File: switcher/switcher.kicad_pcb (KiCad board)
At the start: 2 copper layers, 50 x 100 mm, 61 parts, among them J1 DCDC, J10 GP3, J11 I1, J12 I2, J13 I3, J14 Barrel_Jack_Switch, J2 USB_B_Micro, J3 Power, J4 UART, J5 O1, J6 O2, J7 O3, J8 GP1, J9 GP2, Q1 BC549, Q2 BC549, Q3 BC549, Q4 BC549, Q5 BC549, Q8 BC549, U1 ESP-12E

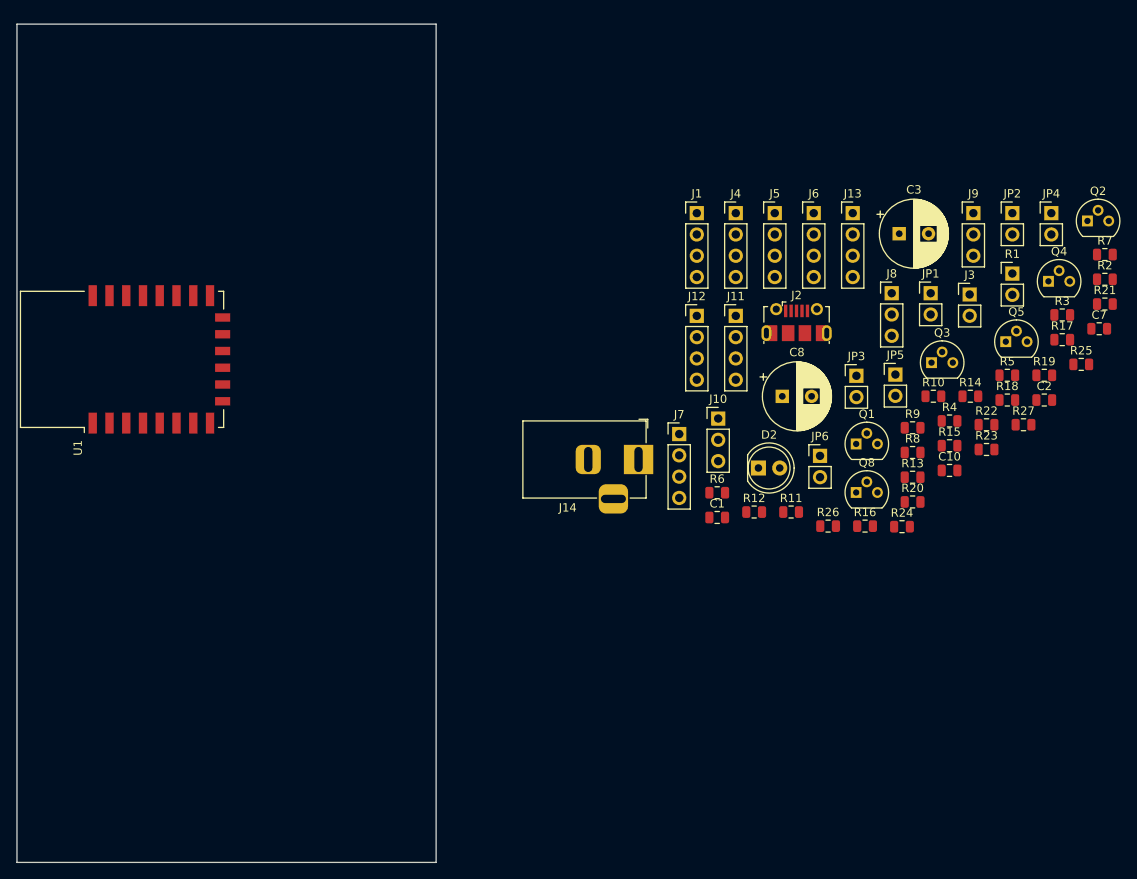
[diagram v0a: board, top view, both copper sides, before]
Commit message: finish the switcher pcb
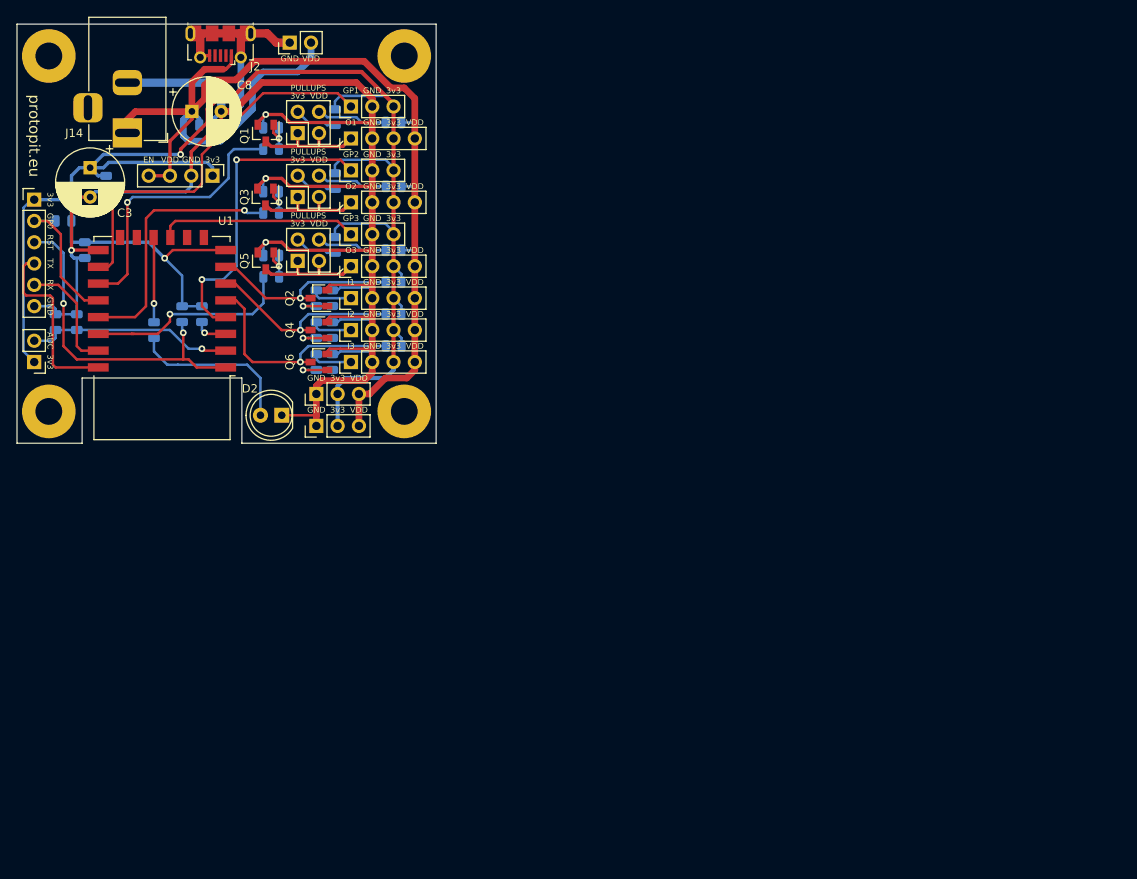
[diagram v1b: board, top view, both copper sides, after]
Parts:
- removed JP4, JP6: USE_VDD, Connector_PinHeader_2.54mm:PinHeader_1x02_P2.54mm_Vertical
- removed JP5: USE_3v3, Connector_PinHeader_2.54mm:PinHeader_1x02_P2.54mm_Vertical
- removed Q8: BC549, Package_TO_SOT_THT:TO-92
- added J16: POWER_OUT, Connector_PinHeader_2.54mm:PinHeader_1x03_P2.54mm_Vertical, F.Cu at (79.7, 100.3)
- added J17: DEBUG, Connector_PinHeader_2.54mm:PinHeader_1x06_P2.54mm_Vertical, F.Cu at (46.0, 73.3)
- added Q6: BC817, Package_TO_SOT_SMD:SOT-23, F.Cu at (80.0, 92.7)
- added REF**: MountingHole_3.2mm_M3_Pad, MountingHole:MountingHole_3.2mm_M3_Pad, F.Cu at (90.2, 98.6)
- added REF**: MountingHole_3.2mm_M3_Pad, MountingHole:MountingHole_3.2mm_M3_Pad, F.Cu at (47.8, 98.6)
- added REF**: MountingHole_3.2mm_M3_Pad, MountingHole:MountingHole_3.2mm_M3_Pad, F.Cu at (47.8, 56.2)
- added REF**: MountingHole_3.2mm_M3_Pad, MountingHole:MountingHole_3.2mm_M3_Pad, F.Cu at (90.2, 56.2)
- C1, C10, C2, C7, R10, R11, R12, R13, R14, R15, R16, R17, R18, R19, R2, R20, R21, R22, R23, R24, R25, R26, R27, R3, R4, R5, R6, R7, R8, R9: moved to B.Cu
- J4: value UART -> POWER_OUT; footprint Connector_PinHeader_2.54mm:PinHeader_1x04_P2.54mm_Vertical -> Connector_PinHeader_2.54mm:PinHeader_1x03_P2.54mm_Vertical
- JP1, JP3: value USE_3v3 -> VSEL; footprint Connector_PinHeader_2.54mm:PinHeader_1x02_P2.54mm_Vertical -> Connector_PinHeader_2.54mm:PinHeader_2x02_P2.54mm_Vertical
- JP2: value USE_VDD -> VSEL; footprint Connector_PinHeader_2.54mm:PinHeader_1x02_P2.54mm_Vertical -> Connector_PinHeader_2.54mm:PinHeader_2x02_P2.54mm_Vertical
- Q1, Q2, Q3, Q4, Q5: value BC549 -> BC817; footprint Package_TO_SOT_THT:TO-92 -> Package_TO_SOT_SMD:SOT-23
- moved R2 125.3 mm to (48.6, 87.9), turned to 90 degrees
- moved R1 117.2 mm to (46.0, 92.7), turned to 180 degrees
- moved C2 114.9 mm to (54.6, 71.4), turned to -90 degrees
- moved R5 114.1 mm to (49.5, 75.9)
- moved C7 109.2 mm to (66.7, 64.4)
- moved C10 105.6 mm to (51.1, 87.9), turned to 90 degrees
- moved R3 105.0 mm to (63.7, 87.0), turned to 90 degrees
- moved R21 101.7 mm to (74.3, 64.8), turned to 180 degrees
- moved C3 96.8 mm to (52.7, 69.5), turned to -90 degrees
- moved R19 96.1 mm to (74.3, 67.3), turned to 180 degrees
- moved R7 94.2 mm to (79.7, 85.1), turned to 90 degrees
- moved Q2 92.1 mm to (80.0, 85.1), turned to 180 degrees
- moved R25 90.2 mm to (81.9, 78.7), turned to -90 degrees
- moved R4 90.1 mm to (66.0, 87.0), turned to 90 degrees
- moved R18 89.0 mm to (74.3, 82.5), turned to 180 degrees
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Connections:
- J4 pad 1: +3V3 -> GND
- J4 pad 2: /ESP_TX -> +3V3
- J4 pad 3: /ESP_RX -> VDD
- JP1 pad 1: Net-(JP1-Pad1) -> /O1
- JP1 pad 2: +3V3 -> Net-(JP1-Pad2)
- JP2 pad 1: Net-(JP2-Pad1) -> /O2
- JP2 pad 2: VDD -> Net-(JP2-Pad2)
- JP3 pad 1: Net-(JP3-Pad1) -> /O3
- JP3 pad 2: +3V3 -> Net-(JP3-Pad2)
- Q1 pad 1: /GPI1 -> Net-(Q1-Pad1)
- Q1 pad 2: Net-(Q1-Pad2) -> GND
- Q1 pad 3: GND -> /O1
- Q2 pad 1: /O2 -> Net-(Q2-Pad1)
- Q2 pad 2: Net-(Q2-Pad2) -> GND
- Q2 pad 3: GND -> /GPI1
- Q3 pad 1: /GPI2 -> Net-(Q3-Pad1)
- Q3 pad 2: Net-(Q3-Pad2) -> GND
- Q3 pad 3: GND -> /O2
- Q4 pad 1: /O3 -> Net-(Q4-Pad1)
- Q4 pad 2: Net-(Q4-Pad2) -> GND
- Q4 pad 3: GND -> /GPI2
- Q5 pad 1: /GPI3 -> Net-(Q5-Pad1)
- Q5 pad 2: Net-(Q5-Pad2) -> GND
- Q5 pad 3: GND -> /O3
- R10 pad 1: Net-(JP2-Pad1) -> VDD
- R10 pad 2: /O1 -> Net-(JP1-Pad4)
- R11 pad 1: Net-(Q2-Pad2) -> Net-(Q3-Pad1)
- R12 pad 1: Net-(Q3-Pad2) -> Net-(Q4-Pad1)
- R13 pad 1: Net-(Q2-Pad2) -> Net-(Q3-Pad1)
- R14 pad 1: Net-(Q3-Pad2) -> Net-(Q4-Pad1)
- R15 pad 1: Net-(JP3-Pad1) -> +3V3
- R15 pad 2: /O2 -> Net-(JP2-Pad2)
- R17 pad 1: Net-(JP4-Pad1) -> VDD
- R17 pad 2: /O2 -> Net-(JP2-Pad4)
- R18 pad 1: Net-(Q4-Pad2) -> Net-(Q5-Pad1)
- R19 pad 1: Net-(Q8-Pad2) -> Net-(Q1-Pad1)
- R20 pad 1: Net-(Q5-Pad2) -> Net-(Q6-Pad1)
- R21 pad 1: Net-(Q8-Pad2) -> Net-(Q1-Pad1)
- R22 pad 1: Net-(Q4-Pad2) -> Net-(Q5-Pad1)
- R23 pad 1: Net-(JP1-Pad1) -> +3V3
- R23 pad 2: /O1 -> Net-(JP1-Pad2)
- R24 pad 1: Net-(Q5-Pad2) -> Net-(Q6-Pad1)
- R25 pad 1: Net-(JP5-Pad1) -> +3V3
- R25 pad 2: /O3 -> Net-(JP3-Pad2)
- R27 pad 1: Net-(JP6-Pad1) -> VDD
- R27 pad 2: /O3 -> Net-(JP3-Pad4)
- R7 pad 1: Net-(Q1-Pad2) -> Net-(Q2-Pad1)
- R8 pad 1: Net-(Q1-Pad2) -> Net-(Q2-Pad1)
- U1 pad 6: /GPI1 -> /GPI2
- U1 pad 7: /GPI2 -> /GPI1
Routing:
- net GND: track 0.00 -> 245.6 mm, vias 0 -> 4
- net +3V3: track 0.00 -> 204.7 mm, vias 0 -> 2
- net VDD: track 0.00 -> 145.7 mm
- net /GP1: track 0.00 -> 46.6 mm
- net /ESP_RST: track 0.00 -> 39.9 mm, vias 0 -> 2
- net /GP2: track 0.00 -> 38.2 mm, vias 0 -> 2
- net /GPO1: track 0.00 -> 33.0 mm, vias 0 -> 1
- net /GPO2: track 0.00 -> 31.2 mm, vias 0 -> 1
- net /GPI3: track 0.00 -> 28.2 mm, vias 0 -> 1
- net /GPO3: track 0.00 -> 25.2 mm, vias 0 -> 1
- net Net-(C10-Pad1): track 0.00 -> 24.8 mm, vias 0 -> 1
- net /GPI2: track 0.00 -> 24.0 mm, vias 0 -> 1
- net /GP3: track 0.00 -> 23.8 mm
- net /GPI1: track 0.00 -> 23.2 mm, vias 0 -> 1
- net /ESP_TX: track 0.00 -> 22.0 mm
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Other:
- board size 50 x 100 mm -> 50 x 50 mm
- board text added: "3v3"
- board text added: "ADC"
- board text added: "EN"
- board text added: "GND"
- board text added: "GP0"
- board text added: "GP1"
- board text added: "GP2"
- board text added: "GP3"
- board text added: "I1"
- board text added: "I2"
- board text added: "I3"
- board text added: "O1"
- board text added: "O2"
- board text added: "O3"
- board text added: "PULLUPS"
- board text added: "RST"
- board text added: "RX"
- board text added: "TX"
- board text added: "VDD"
- board text added: "protopit.eu"

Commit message: driver_motor library and some changes to switcher
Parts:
- J10: value GP3 -> O1; footprint Connector_PinHeader_2.54mm:PinHeader_1x03_P2.54mm_Vertical -> Connector_PinHeader_2.54mm:PinHeader_1x04_P2.54mm_Vertical
- J8: value GP1 -> O1; footprint Connector_PinHeader_2.54mm:PinHeader_1x03_P2.54mm_Vertical -> Connector_PinHeader_2.54mm:PinHeader_1x04_P2.54mm_Vertical
- J9: value GP2 -> O1; footprint Connector_PinHeader_2.54mm:PinHeader_1x03_P2.54mm_Vertical -> Connector_PinHeader_2.54mm:PinHeader_1x04_P2.54mm_Vertical

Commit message: update 0805 components to have larger pads
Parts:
- C1, C10, C2, C7: footprint Capacitor_SMD:C_0805_2012Metric -> Capacitor_SMD:C_0805_2012Metric_Pad1.15x1.40mm_HandSolder
- R10, R11, R12, R13, R14, R15, R16, R17, R18, R19, R2, R20, R21, R22, R23, R24, R25, R26, R27, R3, R4, R5, R6, R7, R8, R9: footprint Resistor_SMD:R_0805_2012Metric -> Resistor_SMD:R_0805_2012Metric_Pad1.15x1.40mm_HandSolder
